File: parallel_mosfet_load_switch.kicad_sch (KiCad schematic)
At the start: 3 parts, among them J1 Conn_02x04_Counter_Clockwise, J2 Conn_02x04_Counter_Clockwise, J3 Conn_02x04_Counter_Clockwise

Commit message: restructered
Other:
- sheet mosfets ports: added VIN; removed none
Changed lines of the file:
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@@
+			)
+		)
+		(pin "VIN" input
+			(at 151.13 67.31 0)
+			(effects
+				(font
+					(size 1.27 1.27)
+				)
+				(justify right)
 			)
 		)

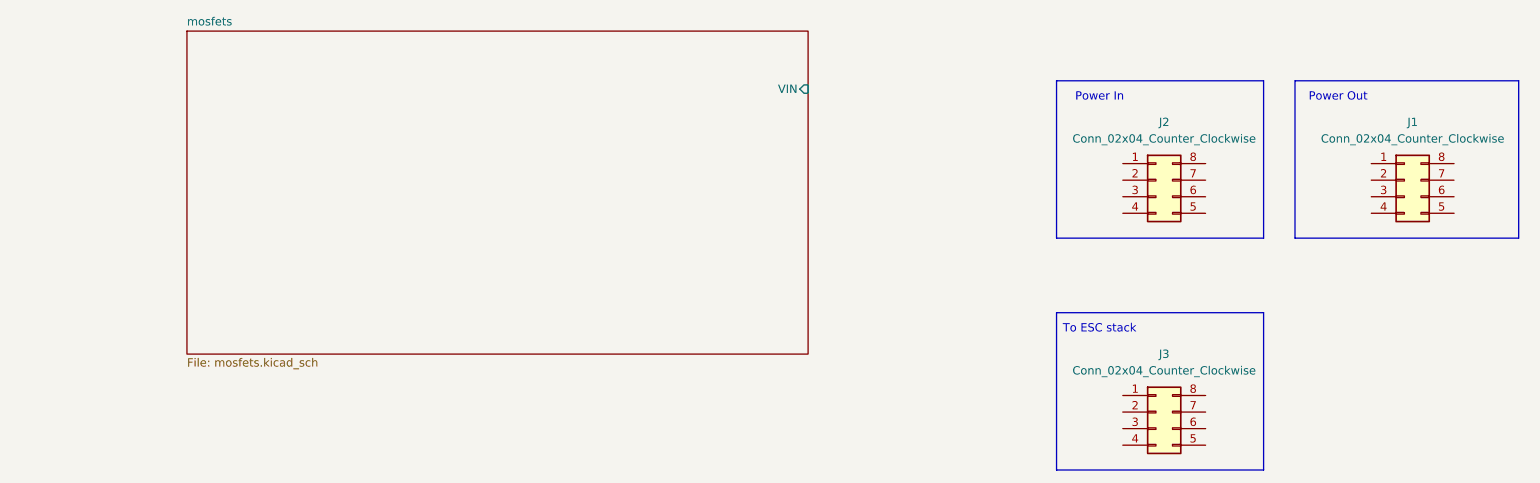
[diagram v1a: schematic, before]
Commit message: changed connectors, cleaned up schematic
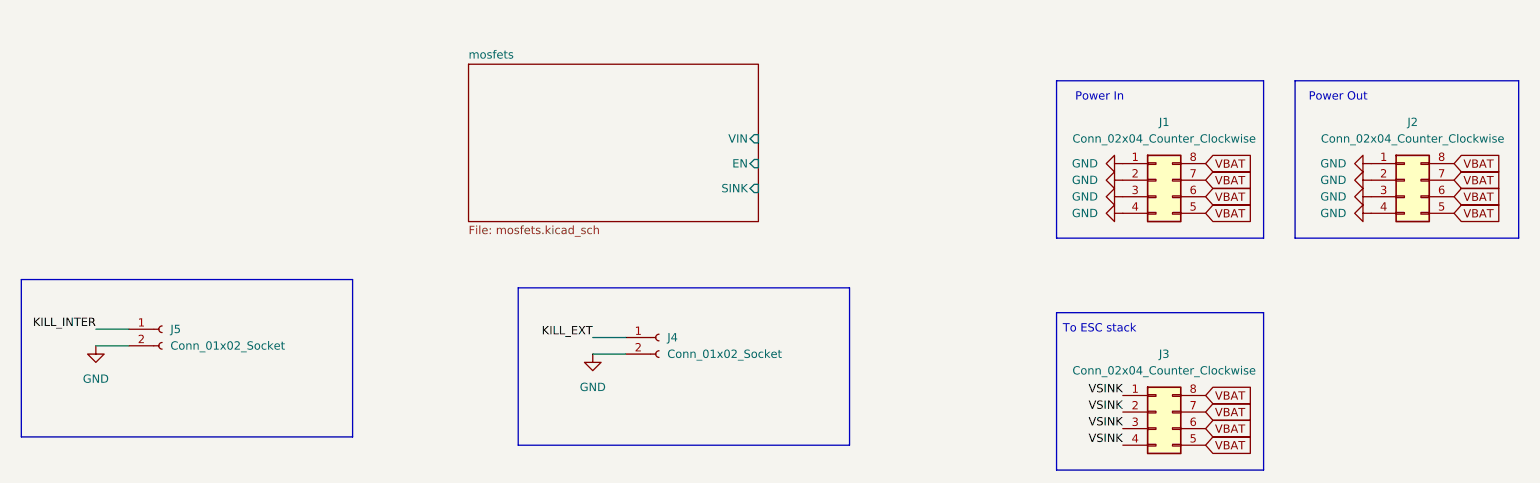
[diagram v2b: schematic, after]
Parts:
- added J4: Conn_01x02_Socket, Connector_PinHeader_2.54mm:PinHeader_1x02_P2.54mm_Vertical, symbol Connector:Conn_01x02_Socket
- added J5: Conn_01x02_Socket, Connector_JST:JST_PH_B2B-PH-K_1x02_P2.00mm_Vertical, symbol Connector:Conn_01x02_Socket
- J1: renamed from J2; footprint (none) -> Connector_Molex:Molex_Mini-Fit_Jr_5569-08A2_2x04_P4.20mm_Horizontal
- J2: renamed from J1; footprint (none) -> Connector_Molex:Molex_Mini-Fit_Jr_5569-08A2_2x04_P4.20mm_Horizontal
- J3: footprint (none) -> Connector_Molex:Molex_Mini-Fit_Jr_5569-08A2_2x04_P4.20mm_Horizontal
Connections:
- net GND: now reaches J1.1 (Pin_1)
- net GND: now also J1.2 (Pin_2), J1.3 (Pin_3), J1.4 (Pin_4), J2.1 (Pin_1), J2.2 (Pin_2), J2.3 (Pin_3), J2.4 (Pin_4), J4.2 (Pin_2), J5.2 (Pin_2)
- net VBAT: now reaches J1.5 (Pin_5)
- net VBAT: now also J1.6 (Pin_6), J1.7 (Pin_7), J1.8 (Pin_8), J2.5 (Pin_5), J2.6 (Pin_6), J2.7 (Pin_7), J2.8 (Pin_8), J3.5 (Pin_5), J3.6 (Pin_6), J3.7 (Pin_7), J3.8 (Pin_8)
- net VSINK: now reaches J3.1 (Pin_1)
- net VSINK: now also J3.2 (Pin_2), J3.3 (Pin_3), J3.4 (Pin_4)
- new net KILL_EXT: J4.1 (Pin_1)
- new net KILL_INTER: J5.1 (Pin_1)
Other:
- sheet mosfets ports: added EN, SINK; removed none
